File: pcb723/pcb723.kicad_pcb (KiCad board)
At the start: 4 copper layers, 90 x 70 mm, 71 parts, among them J1 Conn_01x02_Pin, J10 Conn_01x05_Socket, J11 Conn_01x05_Socket, J2 Conn_01x02_Pin, J3 Conn_02x07_Odd_Even, J4 Conn_02x02_Odd_Even, J5 USB_C_Receptacle_USB2.0_16P, J6 Conn_02x13_Odd_Even, J7 Conn_02x14_Odd_Even, J8 Conn_02x13_Odd_Even, J9 Conn_02x12_Odd_Even, SW1 SW_Push, U1 STM32H723ZGT6, U2 AMS1117-3.3, Y1 8MHz 20pF

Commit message: Route USB-C connector
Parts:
- moved R12 6.44 mm to (167.3, 55.4), turned to 90 degrees
- moved R14 3.75 mm to (166.3, 52.0)
- moved R11 2.05 mm to (174.8, 66.5), turned to -90 degrees
- moved R13 1.00 mm to (176.2, 66.5)
- moved C26 0.37 mm to (177.6, 66.5)
- moved J8 0.29 mm to (98.5, 60.6)
- moved D1 0.06 mm to (169.3, 52.0), turned to 0 degrees
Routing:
- net +5V: track 11.3 -> 51.8 mm, vias 0 -> 1
- net /USB_FS_P: track 0.00 -> 35.7 mm
- net /USB_FS_N: track 0.00 -> 35.7 mm
- net /T_SWDIO: track 0.00 -> 26.6 mm
- net /T_JTDI: track 0.00 -> 25.4 mm
- net /T_SWCLK: track 0.00 -> 22.6 mm
- net Net-(J5-SHIELD): track 0.00 -> 21.5 mm
- net +3V3: track 43.5 -> 61.5 mm, vias 4 -> 9
- net GND: track 31.9 -> 46.2 mm, vias 13 -> 23
- net Net-(J5-CC1): track 0.00 -> 8.01 mm
- net Net-(J5-CC2): track 0.00 -> 6.06 mm
- net Net-(D1-K): track 0.00 -> 1.74 mm
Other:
- board text added: "3V3"
- board text added: "5V"
- board text removed: "3v3"

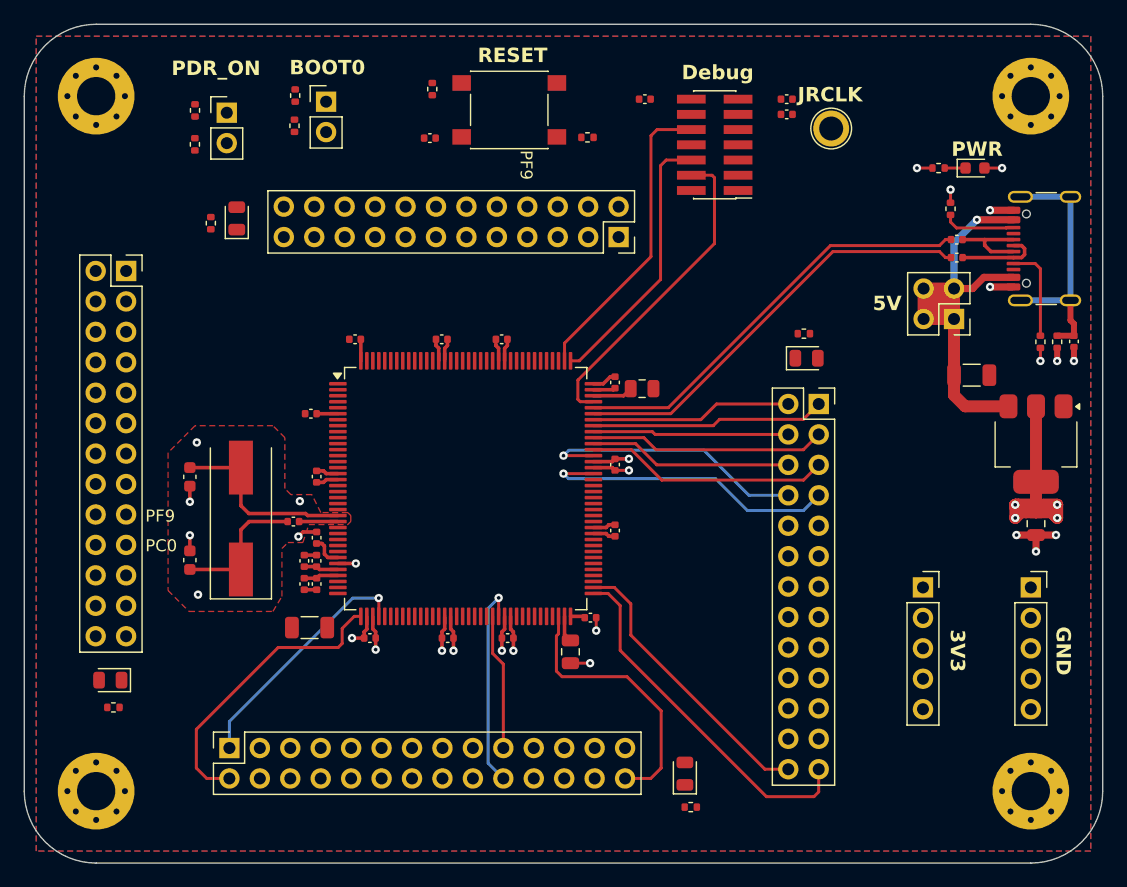
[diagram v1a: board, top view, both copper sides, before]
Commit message: Route LED4
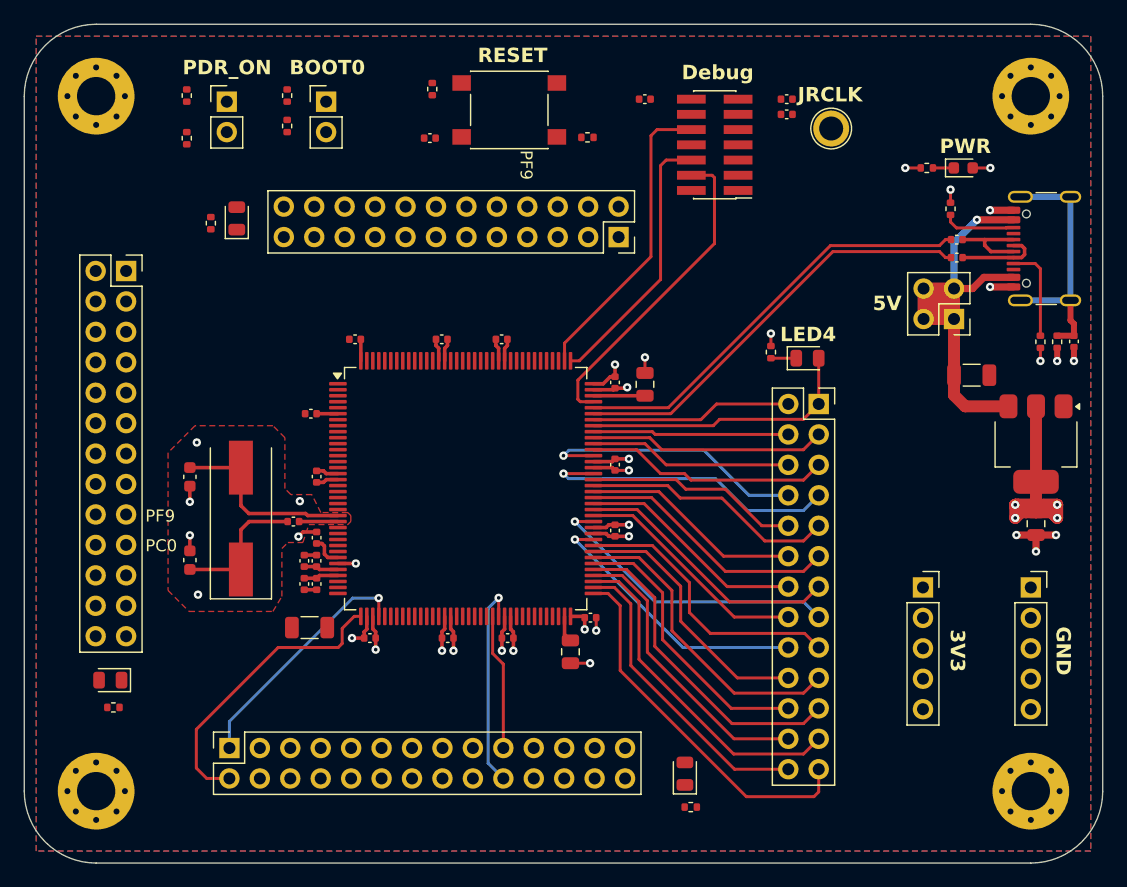
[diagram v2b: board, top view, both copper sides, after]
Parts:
- moved R19 3.15 mm to (152.3, 67.4), turned to 90 degrees
- moved R4 1.42 mm to (103.6, 46.0)
- moved R14 0.98 mm to (165.3, 52.0)
- moved D1 0.98 mm to (168.4, 52.0)
- moved J2 0.92 mm to (106.9, 46.5)
- moved R3 0.85 mm to (103.6, 49.5)
- moved R2 0.67 mm to (111.9, 46.0)
- moved R1 0.61 mm to (111.9, 48.5)
- moved C19 0.43 mm to (141.8, 70.0), turned to -90 degrees
- moved D4 0.07 mm to (155.4, 67.9)
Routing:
- net /PB14: track 0.00 -> 28.1 mm
- net /PD8: track 0.00 -> 27.0 mm
- net /PD10: track 0.00 -> 26.0 mm
- net /PD14: track 0.00 -> 25.2 mm, vias 0 -> 1
- net /PB15: track 0.00 -> 24.4 mm
- net /PD12: track 0.00 -> 23.8 mm
- net /PD9: track 0.00 -> 23.6 mm
- net /PD13: track 0.00 -> 23.1 mm, vias 0 -> 1
- net /PB11: track 22.9 -> 0.00 mm
- net /PG2: track 0.00 -> 22.5 mm
- net /PD11: track 0.00 -> 22.3 mm
- net /PG4: track 0.00 -> 21.9 mm
- net /PG6: track 0.00 -> 21.2 mm
- net /PD15: track 0.00 -> 19.8 mm
- net /PG3: track 0.00 -> 19.1 mm
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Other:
- board text added: "LED4"

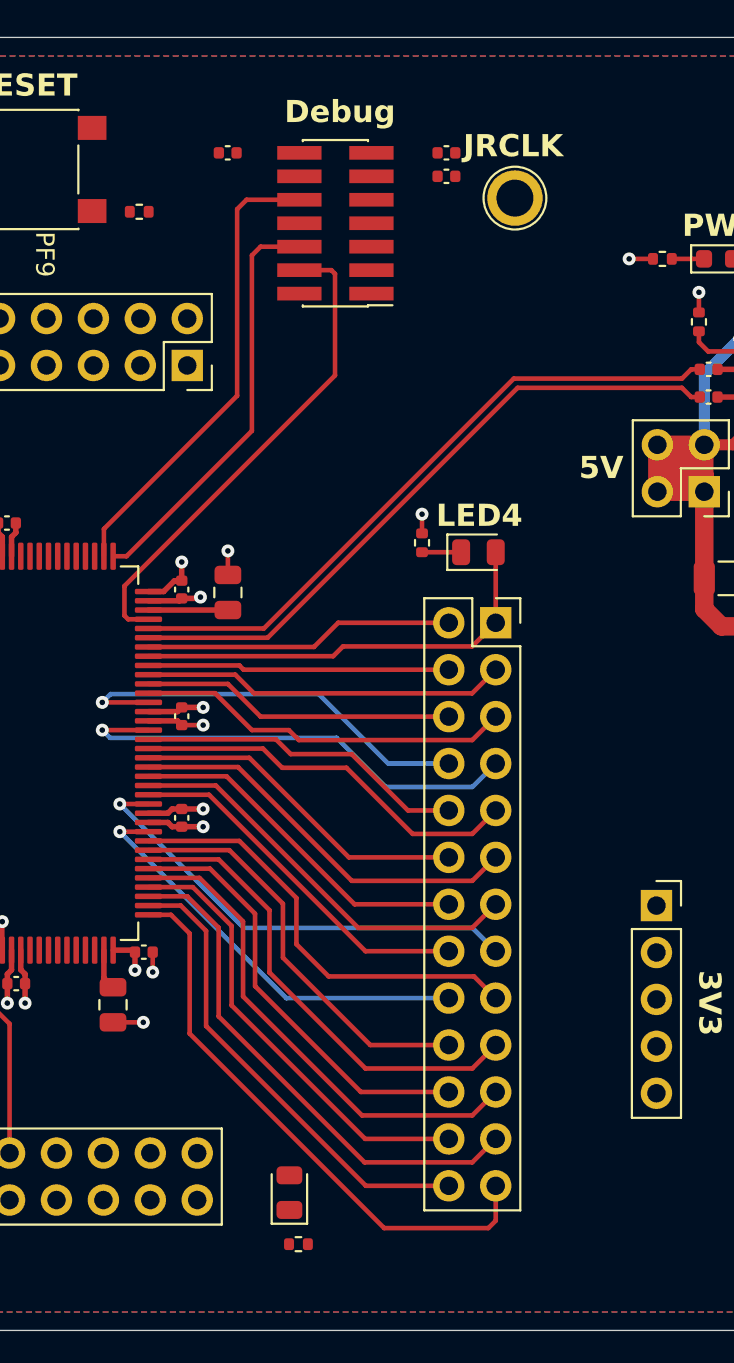
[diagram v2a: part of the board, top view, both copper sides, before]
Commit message: Move JTAG connector higher
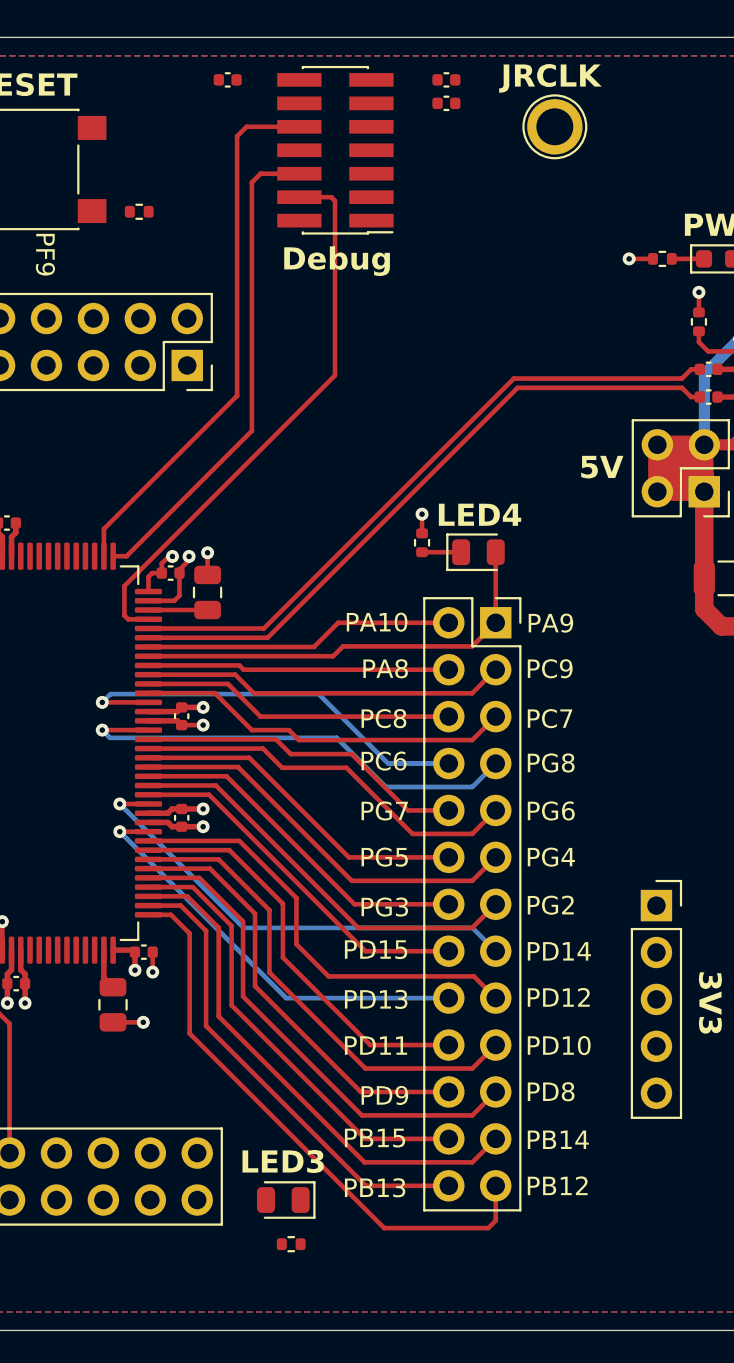
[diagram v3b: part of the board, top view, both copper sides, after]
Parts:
- moved TP1 4.42 mm to (159.5, 44.8)
- moved J3 3.95 mm to (147.6, 46.1)
- moved R10 3.95 mm to (153.6, 42.3)
- moved R8 3.95 mm to (153.6, 43.6)
- moved R9 3.95 mm to (141.8, 42.3)
- moved C19 1.10 mm to (140.7, 70.0)
- moved C8 1.07 mm to (138.7, 69.0), turned to 180 degrees
- moved D2 0.52 mm to (144.8, 102.9), turned to 180 degrees
- moved R17 0.39 mm to (145.2, 105.3), turned to 180 degrees
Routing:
- net /T_SWDIO: track 26.6 -> 30.6 mm
- net /T_SWCLK: track 22.6 -> 26.5 mm
- net /T_JTDI: track 25.4 -> 29.3 mm
- net GND: track 50.7 -> 51.9 mm
- net Net-(C19-Pad2): track 4.30 -> 3.20 mm
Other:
- board text added: "LED3"
- board text added: "PA10"
- board text added: "PA8"
- board text added: "PA9"
- board text added: "PB12"
- board text added: "PB13"
- board text added: "PB14"
- board text added: "PB15"
- board text added: "PC6"
- board text added: "PC7"
- board text added: "PC8"
- board text added: "PC9"
- board text added: "PD10"
- board text added: "PD11"
- board text added: "PD12"
- board text added: "PD13"
- board text added: "PD14"
- board text added: "PD15"
- board text added: "PD8"
- board text added: "PD9"
- board text added: "PG2"
- board text added: "PG3"
- board text added: "PG4"
- board text added: "PG5"
- board text added: "PG6"
- board text added: "PG7"
- board text added: "PG8"

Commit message: Route LED1
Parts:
- R14, R17, R18, R19, R20: footprint Resistor_SMD:R_0402_1005Metric -> Resistor_SMD:R_0805_2012Metric_Pad1.20x1.40mm_HandSolder
- moved C21 14.5 mm to (137.6, 44.9), turned to 180 degrees
- moved R19 10.3 mm to (162.6, 67.9), turned to 0 degrees
- moved R5 3.19 mm to (137.6, 46.3), turned to 180 degrees
- moved R20 2.66 mm to (106.3, 59.2), turned to 0 degrees
- moved R14 2.12 mm to (163.2, 52.0)
- moved R6 1.95 mm to (123.0, 43.8), turned to 180 degrees
- moved D4 1.88 mm to (157.2, 67.9), turned to 180 degrees
- moved J1 1.85 mm to (115.2, 44.6)
- moved J2 1.85 mm to (106.9, 44.6)
- moved R1 1.85 mm to (111.9, 46.6)
- moved R2 1.85 mm to (111.9, 44.1)
- moved R3 1.85 mm to (103.6, 47.7)
- moved R4 1.85 mm to (103.6, 44.1)
- moved D5 1.79 mm to (106.2, 55.2), turned to 0 degrees
- moved SW1 1.15 mm to (130.5, 46.0)
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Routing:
- net Net-(U1-PB7): track 0.00 -> 54.1 mm, vias 0 -> 2
- net Net-(U1-PB6): track 0.00 -> 49.6 mm, vias 0 -> 2
- net /T_SWO: track 0.00 -> 41.9 mm, vias 0 -> 2
- net /PDR_ON: track 0.00 -> 36.4 mm, vias 0 -> 1
- net /BOOT0: track 0.00 -> 26.8 mm, vias 0 -> 1
- net /T_NRST: track 0.00 -> 24.3 mm
- net /PE0: track 0.00 -> 22.2 mm
- net /PG14: track 0.00 -> 18.6 mm, vias 0 -> 1
- net /PD6: track 0.00 -> 16.9 mm, vias 0 -> 1
- net /PB8: track 0.00 -> 16.5 mm
- net /PB4(NJTRST): track 0.00 -> 15.5 mm
- net /PG15: track 0.00 -> 15.4 mm, vias 0 -> 1
- net /PE1: track 0.00 -> 15.4 mm
- net /PC11: track 0.00 -> 15.2 mm
- net /PG12: track 0.00 -> 14.8 mm
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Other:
- board text added: "LED1"
- board text added: "PB4"
- board text added: "PB8"
- board text added: "PC11"
- board text added: "PD0"
- board text added: "PD2"
- board text added: "PD4"
- board text added: "PD6"
- board text added: "PD7"
- board text added: "PE0"
- board text added: "PG10"
- board text added: "PG12"
- board text added: "PG14"

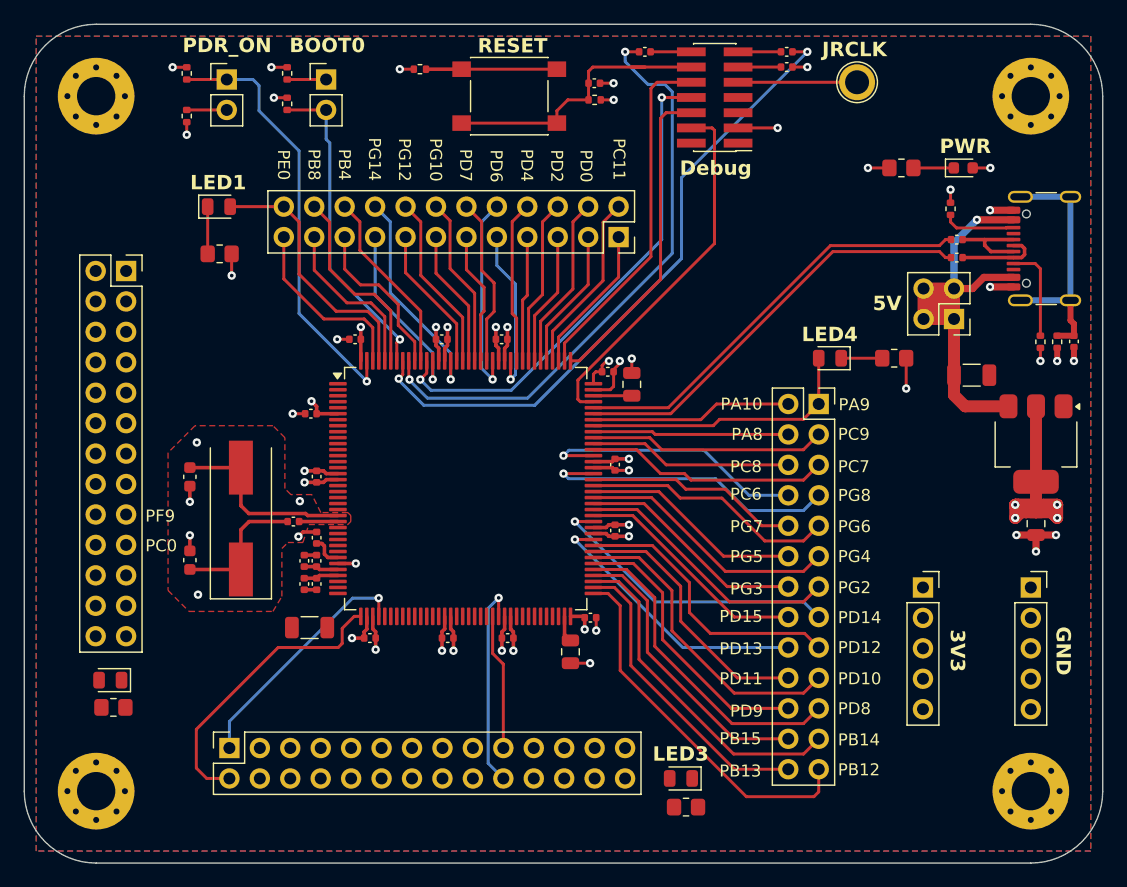
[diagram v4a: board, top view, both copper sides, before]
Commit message: Route LED3
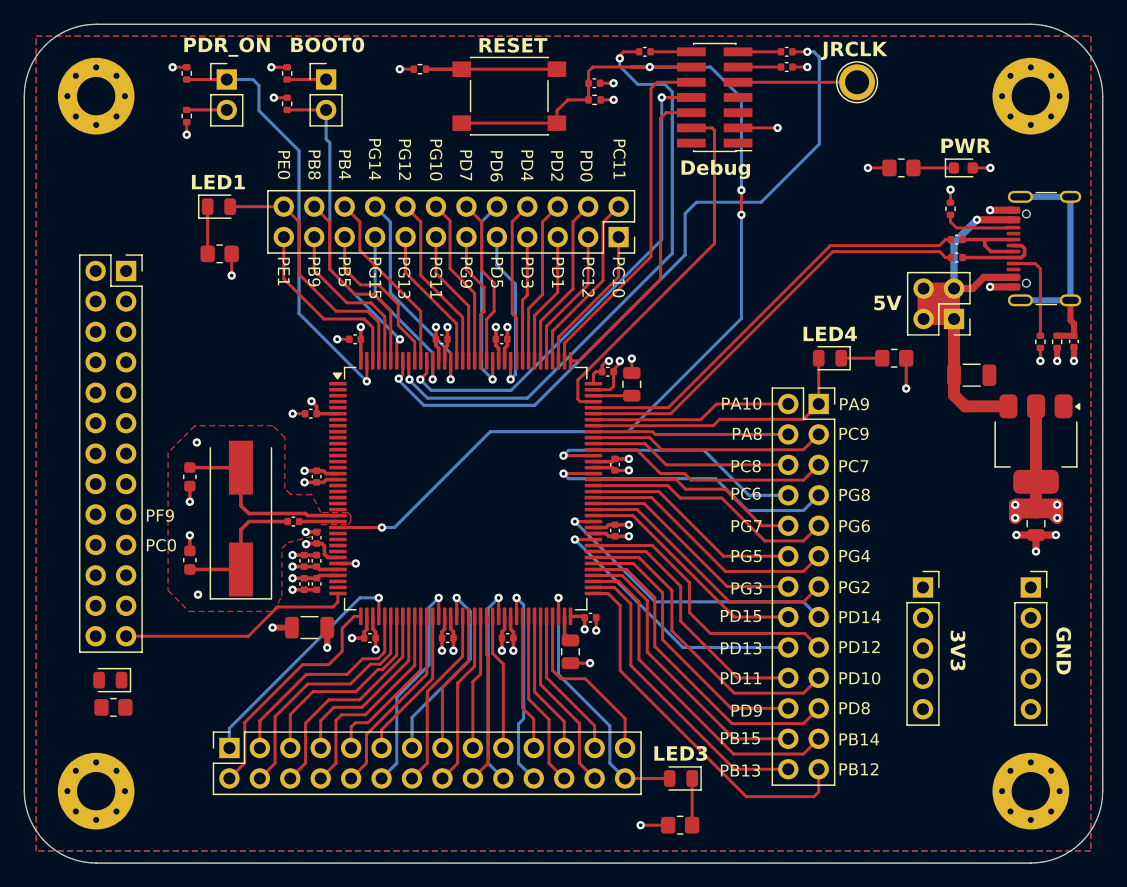
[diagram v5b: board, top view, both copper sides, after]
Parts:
- moved R17 1.59 mm to (144.7, 106.8)
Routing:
- net /T_NRST: track 24.3 -> 92.3 mm, vias 0 -> 4
- net /PB11: track 0.00 -> 22.6 mm, vias 0 -> 1
- net /PA6: track 0.00 -> 20.6 mm
- net /PA2: track 0.00 -> 19.6 mm
- net /PC4: track 0.00 -> 18.9 mm
- net /PF12: track 0.00 -> 18.6 mm, vias 0 -> 1
- net /PA5: track 0.00 -> 18.0 mm
- net /PB0: track 0.00 -> 17.9 mm
- net /PE10: track 0.00 -> 17.6 mm, vias 0 -> 1
- net /PA7: track 0.00 -> 17.0 mm
- net /PF13: track 0.00 -> 16.7 mm, vias 0 -> 1
- net /PB2: track 0.00 -> 16.1 mm
- net /PC5: track 0.00 -> 15.4 mm
- net /PE14: track 0.00 -> 15.4 mm
- net /PF14: track 0.00 -> 15.3 mm
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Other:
- board text added: "PB5"
- board text added: "PB9"
- board text added: "PC10"
- board text added: "PC12"
- board text added: "PD1"
- board text added: "PD3"
- board text added: "PD5"
- board text added: "PE1"
- board text added: "PG11"
- board text added: "PG13"
- board text added: "PG15"
- board text added: "PG9"
